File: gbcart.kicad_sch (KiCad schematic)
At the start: 37 parts, among them J1 Conn_01x32, J2 USB_B_Micro, J3 Micro_SD_Card, J4 Conn_01x06_Male, J5 Conn_01x06_Male, Q1 BC847, SW1 SW_Push, U1 ESP32-S3-MINI-1, U2 74HC138, U3 74HCT1G125, U4 74HC259, U5 29F040-TSOP-SP, U6 74lxc125, U7 74HCT1G125, U8 LD3985M33R_SOT23, U9 NC7SZ08

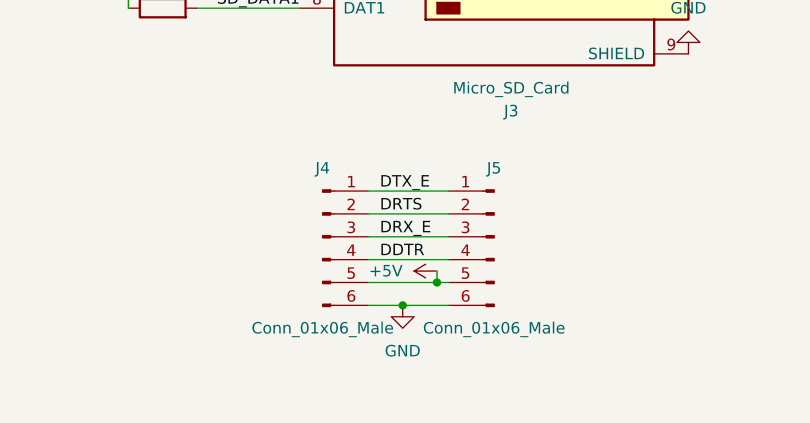
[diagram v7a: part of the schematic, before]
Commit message: Move connector + add silkscren names
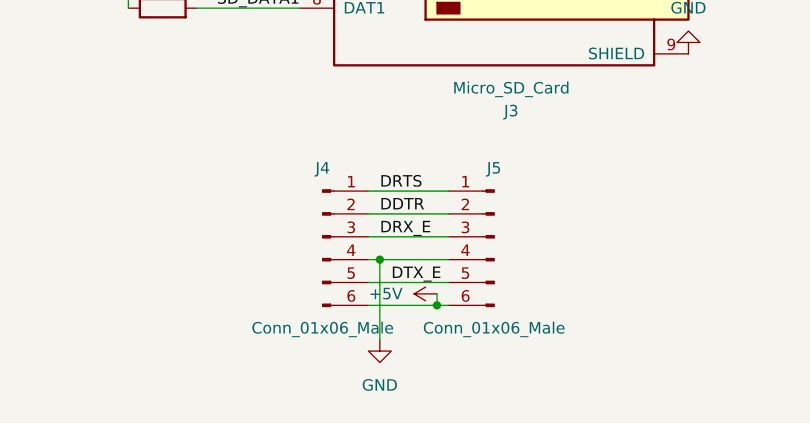
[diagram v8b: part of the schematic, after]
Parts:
- J5: footprint Connector_PinHeader_2.54mm:PinHeader_2x03_P2.54mm_Horizontal -> Connector_PinHeader_2.54mm:PinHeader_2x03_P2.54mm_Vertical
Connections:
- net +5V: now also J4.6 (Pin_6), J5.6 (Pin_6); no longer J4.5 (Pin_5), J5.5 (Pin_5)
- net DDTR: now also J4.2 (Pin_2), J5.2 (Pin_2); no longer J4.4 (Pin_4), J5.4 (Pin_4)
- net DRTS: now also J4.1 (Pin_1), J5.1 (Pin_1); no longer J4.2 (Pin_2), J5.2 (Pin_2)
- net DTX_E: now also J4.5 (Pin_5), J5.5 (Pin_5); no longer J4.1 (Pin_1), J5.1 (Pin_1)
- net GND: now also J4.4 (Pin_4), J5.4 (Pin_4); no longer J4.6 (Pin_6), J5.6 (Pin_6)
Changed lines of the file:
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@@
     (rev "DEV")
   )
+  (junction (at 147.32 182.88) (diameter 0) (color 0 0 0 0)
+  )
   (junction (at 255.27 146.05) (diameter 0) (color 0 0 0 0)
   )
@@
   (junction (at 182.88 125.73) (diameter 0) (color 0 0 0 0)
   )
-  (junction (at 149.86 187.96) (diameter 0) (color 0 0 0 0)
-  )
   (junction (at 215.9 46.99) (diameter 0) (color 0 0 0 0)
   )
+  (junction (at 153.67 187.96) (diameter 0) (color 0 0 0 0)
+  )
   (junction (at 220.98 146.05) (diameter 0) (color 0 0 0 0)
   )
@@
   (junction (at 119.38 142.24) (diameter 0) (color 0 0 0 0)
   )
-  (junction (at 153.67 185.42) (diameter 0) (color 0 0 0 0)
-  )
   (junction (at 242.57 156.21) (diameter 0) (color 0 0 0 0)
   )
@@
     (stroke (width 0) (type default) (color 0 0 0 0))
   )
+  (wire (pts (xy 153.67 186.69) (xy 153.67 187.96))
+    (stroke (width 0) (type default) (color 0 0 0 0))
+  )
   (bus (pts (xy 240.03 41.91) (xy 240.03 44.45))
     (stroke (width 0) (type default) (color 0 0 0 0))
@@
     (stroke (width 0) (type default) (color 0 0 0 0))
   )
-  (wire (pts (xy 153.67 184.15) (xy 153.67 185.42))
-    (stroke (width 0) (type default) (color 0 0 0 0))
-  )
   (wire (pts (xy 120.65 49.53) (xy 127 49.53))
     (stroke (width 0) (type default) (color 0 0 0 0))
@@
     (stroke (width 0) (type default) (color 0 0 0 0))
   )
-  (wire (pts (xy 146.05 187.96) (xy 149.86 187.96))
-    (stroke (width 0) (type default) (color 0 0 0 0))
-  )
   (wire (pts (xy 120.65 34.29) (xy 127 34.29))
     (stroke (width 0) (type default) (color 0 0 0 0))
@@
     (stroke (width 0) (type default) (color 0 0 0 0))
   )
+  (wire (pts (xy 147.32 182.88) (xy 146.05 182.88))
+    (stroke (width 0) (type default) (color 0 0 0 0))
+  )
   (wire (pts (xy 114.3 109.22) (xy 109.22 109.22))
     (stroke (width 0) (type default) (color 0 0 0 0))
@@
     (stroke (width 0) (type default) (color 0 0 0 0))
   )
+  (wire (pts (xy 147.32 182.88) (xy 154.94 182.88))
+    (stroke (width 0) (type default) (color 0 0 0 0))
+  )
   (bus (pts (xy 182.88 22.86) (xy 182.88 59.69))
     (stroke (width 0) (type default) (color 0 0 0 0))
@@
     (stroke (width 0) (type default) (color 0 0 0 0))
   )
+  (wire (pts (xy 147.32 182.88) (xy 147.32 191.77))
+    (stroke (width 0) (type default) (color 0 0 0 0))
+  )
   (wire (pts (xy 127 137.16) (xy 138.43 137.16))
     (stroke (width 0) (type default) (color 0 0 0 0))
@@
     (stroke (width 0) (type default) (color 0 0 0 0))
   )
-  (wire (pts (xy 153.67 185.42) (xy 146.05 185.42))
+  (wire (pts (xy 146.05 185.42) (xy 154.94 185.42))
     (stroke (width 0) (type default) (color 0 0 0 0))
   )
@@
     (stroke (width 0) (type default) (color 0 0 0 0))
   )
+  (wire (pts (xy 153.67 187.96) (xy 154.94 187.96))
+    (stroke (width 0) (type default) (color 0 0 0 0))
+  )
   (wire (pts (xy 69.85 34.29) (xy 69.85 73.66))
     (stroke (width 0) (type default) (color 0 0 0 0))
@@
     (stroke (width 0) (type default) (color 0 0 0 0))
   )
-  (wire (pts (xy 154.94 182.88) (xy 146.05 182.88))
-    (stroke (width 0) (type default) (color 0 0 0 0))
-  )
   (wire (pts (xy 220.98 146.05) (xy 234.95 146.05))
     (stroke (width 0) (type default) (color 0 0 0 0))
@@
     (stroke (width 0) (type default) (color 0 0 0 0))
   )
-  (wire (pts (xy 149.86 187.96) (xy 154.94 187.96))
+  (wire (pts (xy 146.05 187.96) (xy 153.67 187.96))
     (stroke (width 0) (type default) (color 0 0 0 0))
   )
@@
   )
   (bus (pts (xy 182.88 90.17) (xy 182.88 92.71))
-    (stroke (width 0) (type default) (color 0 0 0 0))
-  )
-  (wire (pts (xy 154.94 185.42) (xy 153.67 185.42))
     (stroke (width 0) (type default) (color 0 0 0 0))
   )
@@
     (effects (font (size 1.27 1.27)) (justify left bottom))
   )
-  (label "DRTS" (at 147.32 177.8 0)
+  (label "DRTS" (at 147.32 175.26 0)
     (effects (font (size 1.27 1.27)) (justify left bottom))
   )
@@
     (effects (font (size 1.27 1.27)) (justify right bottom))
   )
-  (label "DDTR" (at 147.32 182.88 0)
+  (label "DDTR" (at 147.32 177.8 0)
     (effects (font (size 1.27 1.27)) (justify left bottom))
   )
@@
     (effects (font (size 1.27 1.27)) (justify right bottom))
   )
-  (label "DTX_E" (at 147.32 175.26 0)
+  (label "DTX_E" (at 148.59 185.42 0)
     (effects (font (size 1.27 1.27)) (justify left bottom))
   )
@@
     (pin "7")
   )
-  (symbol (lib_id "power:+5V") (at 153.67 184.15 90) (unit 1)
-    (in_bom yes) (on_board yes) (fields_autoplaced)
-    (property "Reference" "#PWR0109" (id 0) (at 157.48 184.15 0)
-      (effects (font (size 1.27 1.27)) hide)
-    )
-    (property "Value" "+5V" (id 1) (at 149.86 184.1499 90)
-      (effects (font (size 1.27 1.27)) (justify left))
-    )
-    (property "Footprint" "" (id 2) (at 153.67 184.15 0)
-      (effects (font (size 1.27 1.27)) hide)
-    )
-    (property "Datasheet" "" (id 3) (at 153.67 184.15 0)
+  (symbol (lib_id "power:+5V") (at 153.67 186.69 90) (unit 1)
+    (in_bom yes) (on_board yes) (fields_autoplaced)
+    (property "Reference" "#PWR0109" (id 0) (at 157.48 186.69 0)
+      (effects (font (size 1.27 1.27)) hide)
+    )
+    (property "Value" "+5V" (id 1) (at 149.86 186.6899 90)
+      (effects (font (size 1.27 1.27)) (justify left))
+    )
+    (property "Footprint" "" (id 2) (at 153.67 186.69 0)
+      (effects (font (size 1.27 1.27)) hide)
+    )
+    (property "Datasheet" "" (id 3) (at 153.67 186.69 0)
       (effects (font (size 1.27 1.27)) hide)
     )
@@
   (symbol (lib_id "power:GND") (at 107.95 109.22 180) (unit 1)
     (in_bom yes) (on_board yes) (fields_autoplaced)
-    (property "Reference" "#PWR?" (id 0) (at 107.95 102.87 0)
+    (property "Reference" "#PWR0117" (id 0) (at 107.95 102.87 0)
       (effects (font (size 1.27 1.27)) hide)
     )
@@
     (property "Reference" "J5" (id 0) (at 160.02 172.72 0))
     (property "Value" "Conn_01x06_Male" (id 1) (at 160.02 190.5 0))
-    (property "Footprint" "Connector_PinHeader_2.54mm:PinHeader_2x03_P2.54mm_Horizontal" (id 2) (at 160.02 180.34 0)
+    (property "Footprint" "Connector_PinHeader_2.54mm:PinHeader_2x03_P2.54mm_Vertical" (id 2) (at 160.02 180.34 0)
       (effects (font (size 1.27 1.27)) hide)
     )
@@
     (pin "2")
   )
-  (symbol (lib_id "power:GND") (at 149.86 187.96 0) (unit 1)
-    (in_bom yes) (on_board yes) (fields_autoplaced)
-    (property "Reference" "#PWR0108" (id 0) (at 149.86 194.31 0)
-      (effects (font (size 1.27 1.27)) hide)
-    )
-    (property "Value" "GND" (id 1) (at 149.86 193.04 0))
-    (property "Footprint" "" (id 2) (at 149.86 187.96 0)
-      (effects (font (size 1.27 1.27)) hide)
-    )
-    (property "Datasheet" "" (id 3) (at 149.86 187.96 0)
+  (symbol (lib_id "power:GND") (at 147.32 191.77 0) (unit 1)
+    (in_bom yes) (on_board yes) (fields_autoplaced)
+    (property "Reference" "#PWR0108" (id 0) (at 147.32 198.12 0)
+      (effects (font (size 1.27 1.27)) hide)
+    )
+    (property "Value" "GND" (id 1) (at 147.32 196.85 0))
+    (property "Footprint" "" (id 2) (at 147.32 191.77 0)
+      (effects (font (size 1.27 1.27)) hide)
+    )
+    (property "Datasheet" "" (id 3) (at 147.32 191.77 0)
       (effects (font (size 1.27 1.27)) hide)
     )
@@
       (reference "#PWR0116") (unit 1) (value "GND") (footprint "")
     )
+    (path "/9cee09a3-48cb-4ab6-bee5-1332d5233181"
+      (reference "#PWR0117") (unit 1) (value "GND") (footprint "")
+    )
     (path "/b96670c9-c9f3-4bda-9065-9a56d3e5c5e5"
       (reference "#PWR0119") (unit 1) (value "GND") (footprint "")
     )
-    (path "/9cee09a3-48cb-4ab6-bee5-1332d5233181"
-      (reference "#PWR?") (unit 1) (value "GND") (footprint "")
-    )
     (path "/2d349485-4630-4d56-9137-2d98b8ea5904"
       (reference "C1") (unit 1) (value "10nF") (footprint "Capacitor_SMD:C_0805_2012Metric_Pad1.18x1.45mm_HandSolder")
@@
     )
     (path "/a246aac7-7758-4c8b-bae1-c789bda44567"
-      (reference "J5") (unit 1) (value "Conn_01x06_Male") (footprint "Connector_PinHeader_2.54mm:PinHeader_2x03_P2.54mm_Horizontal")
+      (reference "J5") (unit 1) (value "Conn_01x06_Male") (footprint "Connector_PinHeader_2.54mm:PinHeader_2x03_P2.54mm_Vertical")
     )
     (path "/6adc6610-0951-4465-a386-2d8b22668d9e"
